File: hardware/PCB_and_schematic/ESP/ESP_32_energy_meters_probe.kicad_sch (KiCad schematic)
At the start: 31 parts, among them J19 GAMA_METER, J2 POZYTON_METER, J4 Conn_01x04, J5 Conn_01x04, U16 74HC14, U4 ST485EBDR, U5 ST485EBDR, U6 74HC14

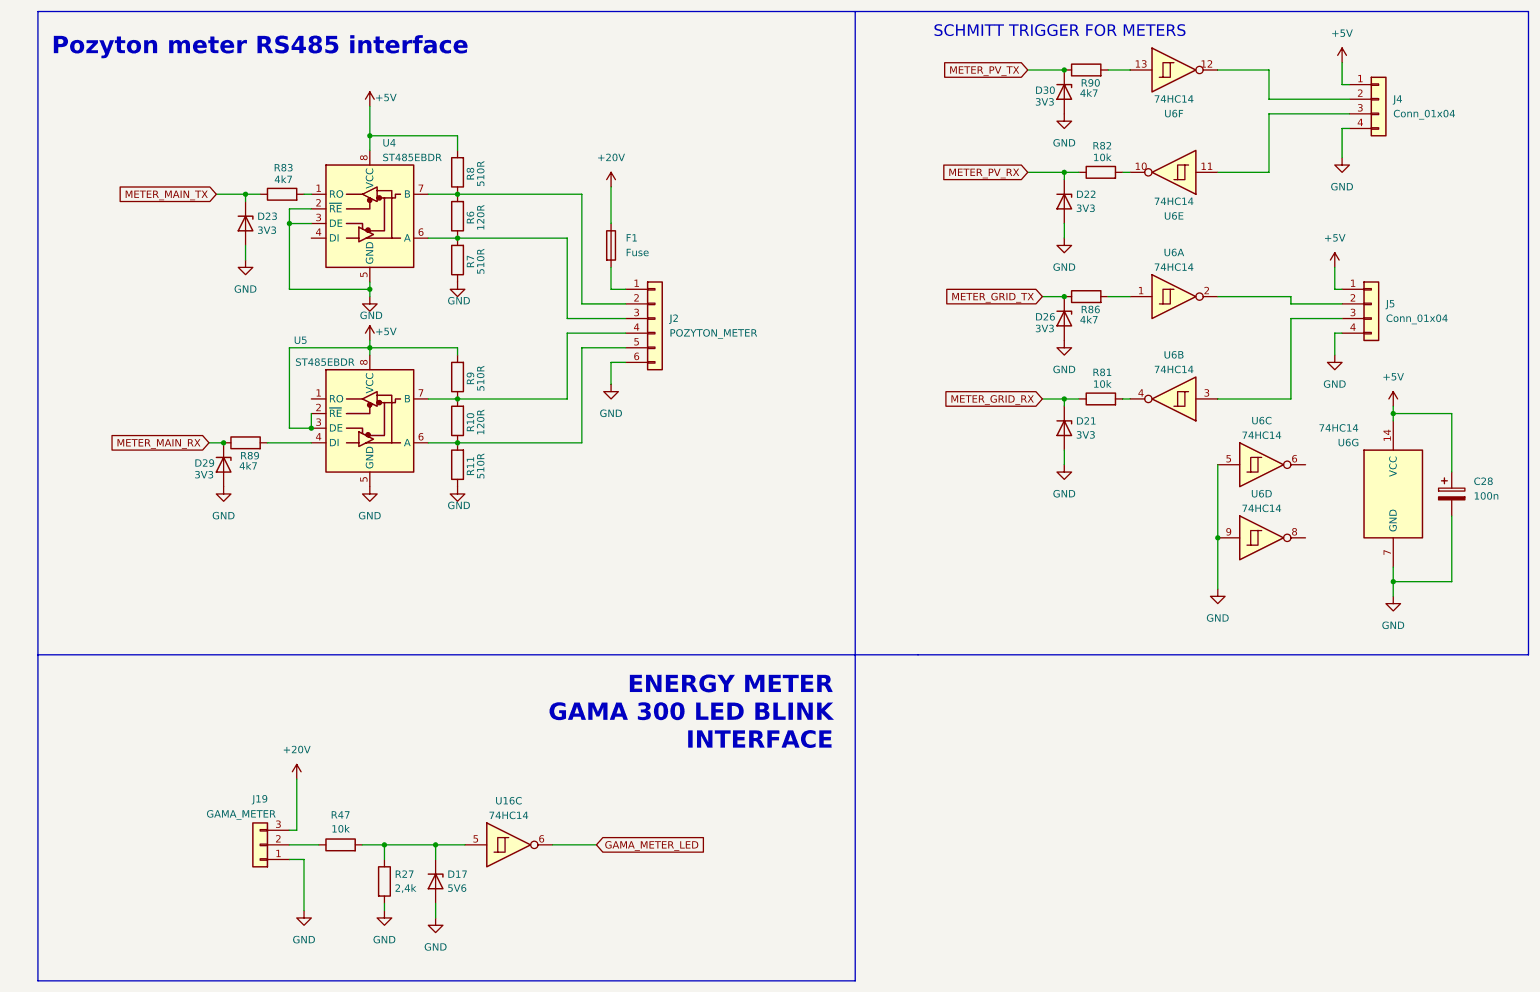
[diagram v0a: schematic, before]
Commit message: Splitter PCB, connectors esp board
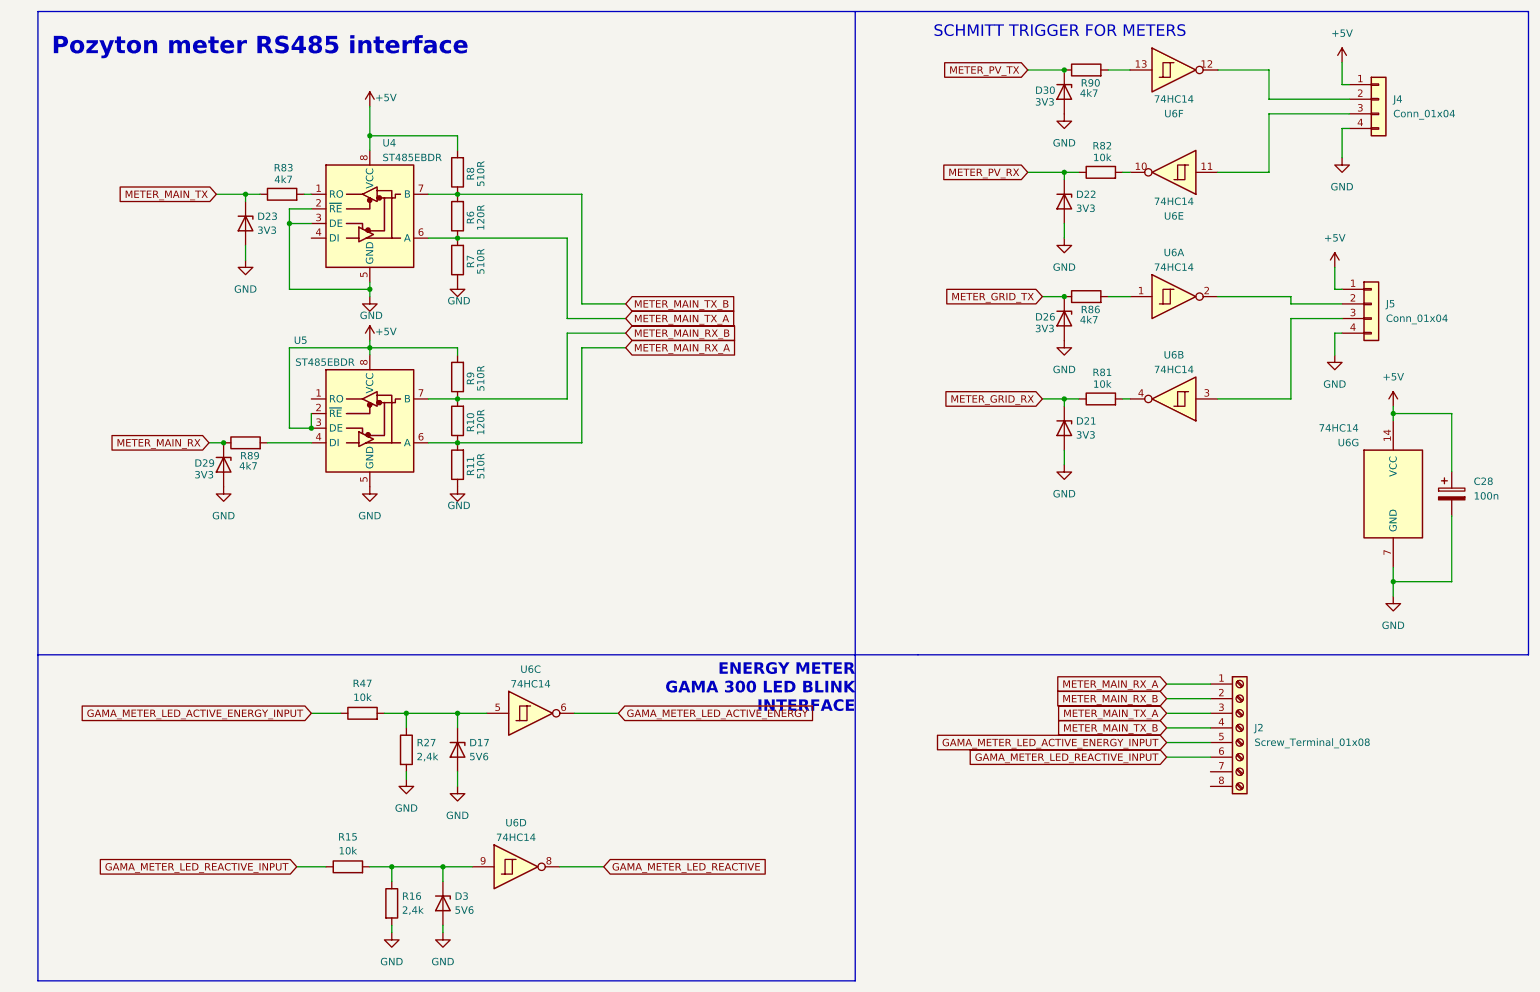
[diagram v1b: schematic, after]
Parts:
- removed F1: Fuse, Fuse:Fuseholder_Clip-5x20mm_Littelfuse_519_Inline_P20.60x5.00mm_D1.00mm_Horizontal, symbol Device:Fuse
- removed J19: GAMA_METER, Connector_PinHeader_2.54mm:PinHeader_1x03_P2.54mm_Vertical, symbol Connector_Generic:Conn_01x03
- removed J2: POZYTON_METER, Connector_JST:JST_EH_B6B-EH-A_1x06_P2.50mm_Vertical, symbol Connector_Generic:Conn_01x06
- removed U16: 74HC14, Package_SO:SOIC-14_3.9x8.7mm_P1.27mm, symbol 74xx:74HC14
- added D3: 5V6, Diode_SMD:D_MiniMELF, symbol Device:D_Zener
- added J2: Screw_Terminal_01x08, TerminalBlock:TerminalBlock_bornier-8_P5.08mm, symbol Connector:Screw_Terminal_01x08
- added R15: 10k, Resistor_SMD:R_0805_2012Metric_Pad1.20x1.40mm_HandSolder, symbol Device:R
- added R16: 2,4k, Resistor_SMD:R_0805_2012Metric_Pad1.20x1.40mm_HandSolder, symbol Device:R
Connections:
- net GND: now also D3.2 (A), R16.2; no longer U6.5, U6.9
- net METER_MAIN_TX_A: now reaches R6.1, R7.2, U4.6 (A)
- net METER_MAIN_TX_A: now also J2.3 (Pin_3)
- net at D17.1 (K), R27.1, R47.2: now also U6.5
- net METER_MAIN_TX_B: now reaches R6.2, R8.1, U4.7 (B)
- net METER_MAIN_TX_B: now also J2.4 (Pin_4)
- net METER_MAIN_RX_B: now reaches R10.2, R9.1, U5.7 (B)
- net METER_MAIN_RX_B: now also J2.2 (Pin_2)
- net METER_MAIN_RX_A: now reaches R10.1, R11.2, U5.6 (A)
- net METER_MAIN_RX_A: now also J2.1 (Pin_1)
- net GAMA_METER_LED_ACTIVE_ENERGY_INPUT: now reaches R47.1
- net GAMA_METER_LED_ACTIVE_ENERGY_INPUT: now also J2.5 (Pin_5)
- net GAMA_METER_LED_ACTIVE_ENERGY: now reaches U6.6
- net GAMA_METER_LED_REACTIVE: now reaches U6.8
- new net: D3.1 (K), R15.2, R16.1, U6.9
- new net GAMA_METER_LED_REACTIVE_INPUT: J2.6 (Pin_6), R15.1
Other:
- moved on the sheet: D17, R27, R47

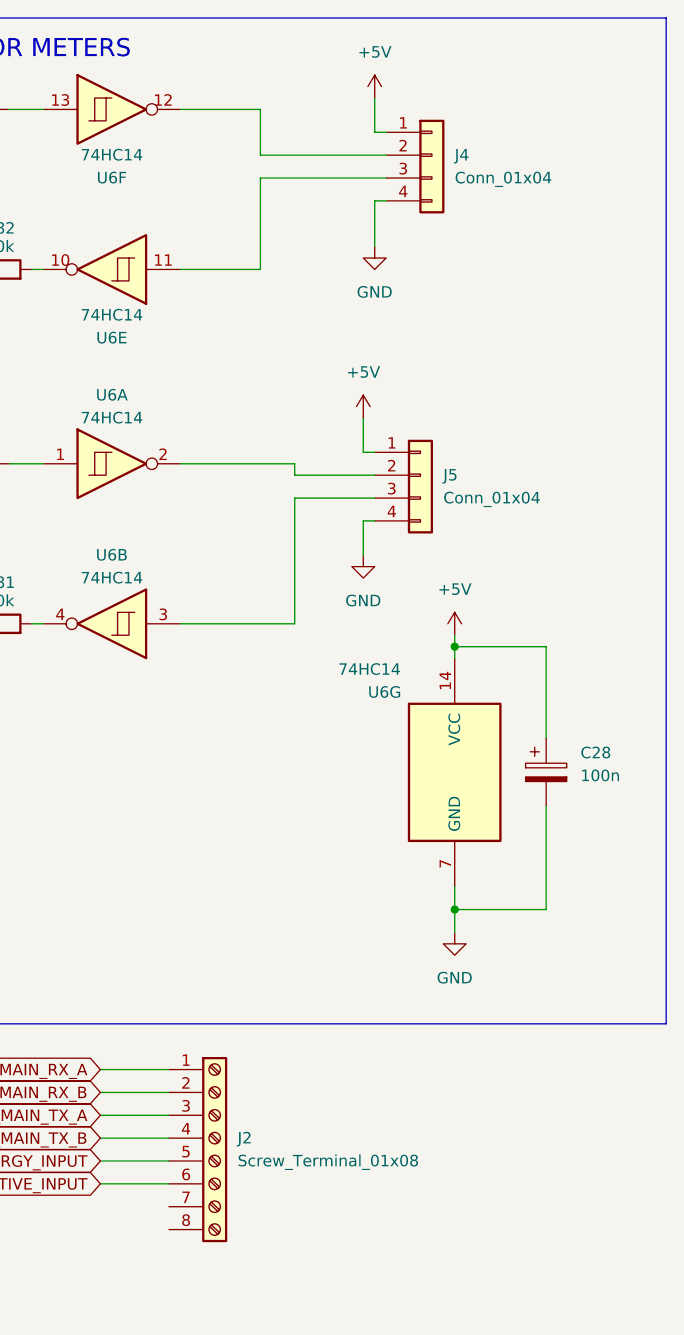
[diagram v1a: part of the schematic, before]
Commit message: Update of ESP32 PCB - parts positioning
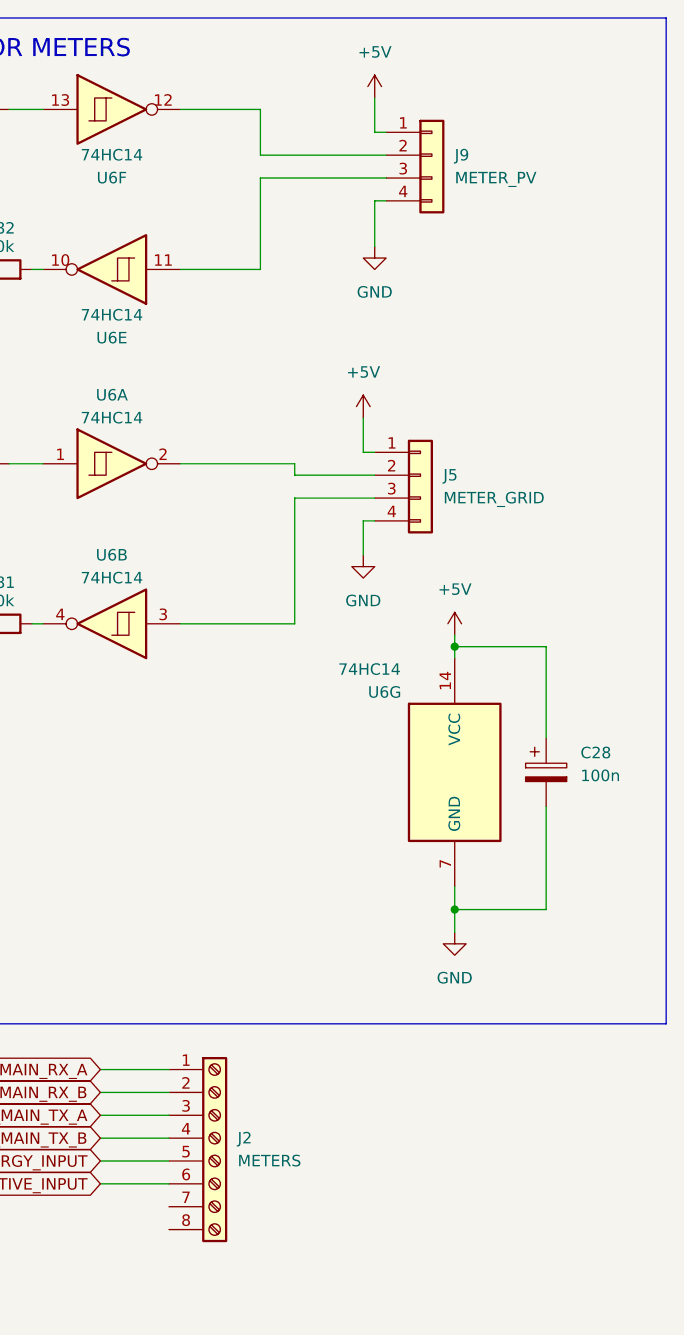
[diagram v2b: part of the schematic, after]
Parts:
- J2: value Screw_Terminal_01x08 -> METERS
- J5: value Conn_01x04 -> METER_GRID
- J9: renamed from J4; value Conn_01x04 -> METER_PV

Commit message: esp pcb
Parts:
- removed J2: METERS, TerminalBlock:TerminalBlock_bornier-8_P5.08mm, symbol Connector:Screw_Terminal_01x08
- added J2: Conn_01x10, My-Footprints-connectors:CDDC-1,5-5-PV-3,5, symbol Connector_Generic:Conn_01x10
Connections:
- net GAMA_METER_LED_ACTIVE_ENERGY_INPUT: now also J2.5 (Pin_5)
- net GAMA_METER_LED_REACTIVE_INPUT: now also J2.6 (Pin_6)
- net METER_MAIN_RX_A: now also J2.1 (Pin_1)
- net METER_MAIN_RX_B: now also J2.2 (Pin_2)
- net METER_MAIN_TX_A: now also J2.3 (Pin_3)
- net METER_MAIN_TX_B: now also J2.4 (Pin_4)
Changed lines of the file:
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@@
+	)
+	(symbol
+		(lib_id "Connector_Generic:Conn_01x10")
+		(at 231.14 144.78 0)
+		(unit 1)
+		(exclude_from_sim no)
+		(in_bom yes)
+		(on_board yes)
+		(dnp no)
+		(fields_autoplaced yes)
+		(property "Reference" "J2"
+			(at 233.172 144.8378 0)
+			(effects
+				(font
+					(size 1.27 1.27)
+				)
+				(justify left)
+			)
+		)
+		(property "Value" "Conn_01x10"
+			(at 233.172 147.2621 0)
+			(effects
+				(font
+					(size 1.27 1.27)
+				)
+				(justify left)
+			)
+		)
+		(property "Footprint" "My-Footprints-connectors:CDDC-1,5-5-PV-3,5"
+			(at 231.14 144.78 0)
+			(effects
+				(font
+					(size 1.27 1.27)
+				)
+				(hide yes)
+			)
+		)
+		(property "Datasheet" "~"
+			(at 231.14 144.78 0)
+			(effects
+				(font
+					(size 1.27 1.27)
+				)
+				(hide yes)
+			)
+		)
+		(property "Description" "Generic connector, single row, 01x10, script generated (kicad-library-utils/schlib/autogen/connector/)"
+			(at 231.14 144.78 0)
+			(effects
+				(font
+					(size 1.27 1.27)
+				)
+				(hide yes)
+			)
+		)
+		(pin "4"
+		)
+		(pin "10"
+		)
+		(pin "5"
+		)
+		(pin "8"
+		)
+		(pin "6"
+		)
+		(pin "9"
+		)
+		(pin "2"
+		)
+		(pin "1"
+		)
+		(pin "3"
+		)
+		(pin "7"
+		)
+		(instances
+			(project "ESP32_master"
+				(path "/555ba40f-9abb-4b99-82c6-07e888fda9fd/8e097fd6-54e8-4c39-b60f-16b9a98546bb"
+					(reference "J2")
+					(unit 1)
+				)
+			)
+		)
 	)
 	(symbol
@@
 					(unit 1)
 				)
-			)
-		)
-	)
-	(symbol
-		(lib_id "Connector:Screw_Terminal_01x08")
-		(at 231.14 142.24 0)
-		(unit 1)
-		(exclude_from_sim no)
-		(in_bom yes)
-		(on_board yes)
-		(dnp no)
-		(fields_autoplaced yes)
-		(property "Reference" "J2"
-			(at 233.68 142.2399 0)
-			(effects
-				(font
-					(size 1.27 1.27)
-				)
-				(justify left)
-			)
-		)
-		(property "Value" "METERS"
-			(at 233.68 144.7799 0)
-			(effects
-				(font
-					(size 1.27 1.27)
-				)
-				(justify left)
-			)
-		)
-		(property "Footprint" "TerminalBlock:TerminalBlock_bornier-8_P5.08mm"
-			(at 231.14 142.24 0)
-			(effects
-				(font
-					(size 1.27 1.27)
-				)
-				(hide yes)
-			)
-		)
-		(property "Datasheet" "~"
-			(at 231.14 142.24 0)
-			(effects
-				(font
-					(size 1.27 1.27)
-				)
-				(hide yes)
-			)
-		)
-		(property "Description" "Generic screw terminal, single row, 01x08, script generated (kicad-library-utils/schlib/autogen/connector/)"
-			(at 231.14 142.24 0)
-			(effects
-				(font
-					(size 1.27 1.27)
-				)
-				(hide yes)
-			)
-		)
-		(pin "6"
-		)
-		(pin "4"
-		)
-		(pin "2"
-		)
-		(pin "7"
-		)
-		(pin "5"
-		)
-		(pin "1"
-		)
-		(pin "3"
-		)
-		(pin "8"
-		)
-		(instances
-			(project "ESP32_master"
-				(path "/555ba40f-9abb-4b99-82c6-07e888fda9fd/8e097fd6-54e8-4c39-b60f-16b9a98546bb"
-					(reference "J2")
-					(unit 1)
-				)

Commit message: Routing PCB
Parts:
- added R35, R36: 0R, Resistor_SMD:R_0805_2012Metric_Pad1.20x1.40mm_HandSolder, symbol Device:R
- J2: value Conn_01x10 -> EXTERNAL_SIGNALS
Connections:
- net +5V: now also J2.5 (Pin_5)
- net GAMA_METER_LED_ACTIVE_ENERGY_INPUT: now also J2.1 (Pin_1); no longer J2.5 (Pin_5)
- net GAMA_METER_LED_REACTIVE_INPUT: now also J2.2 (Pin_2); no longer J2.6 (Pin_6)
- net GND: now also J2.6 (Pin_6)
- net METER_MAIN_RX_A: now also J2.8 (Pin_8); no longer J2.1 (Pin_1)
- net METER_MAIN_RX_B: now also J2.7 (Pin_7); no longer J2.2 (Pin_2)
- net METER_MAIN_TX_A: now also J2.10 (Pin_10); no longer J2.3 (Pin_3)
- net METER_MAIN_TX_B: now also J2.9 (Pin_9); no longer J2.4 (Pin_4)
- new net: J2.3 (Pin_3), R35.2
- new net: J2.4 (Pin_4), R36.2
- new net P6_UNCONNECTED: R36.1
- new net P7_UNCONNECTED: R35.1
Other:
- moved on the sheet: C28, J2, U6G
